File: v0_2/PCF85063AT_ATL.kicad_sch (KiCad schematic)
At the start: 4 parts, among them Q3 DMG2301L-7, U2 PCF85063ATL

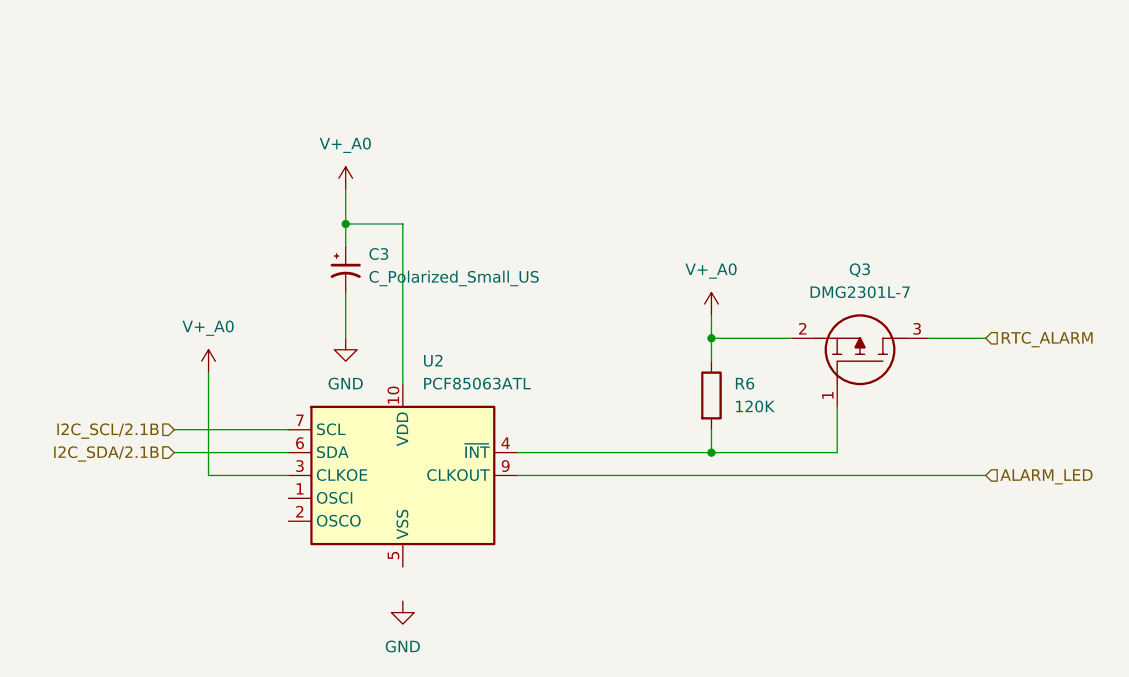
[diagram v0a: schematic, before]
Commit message: add sensor schematic
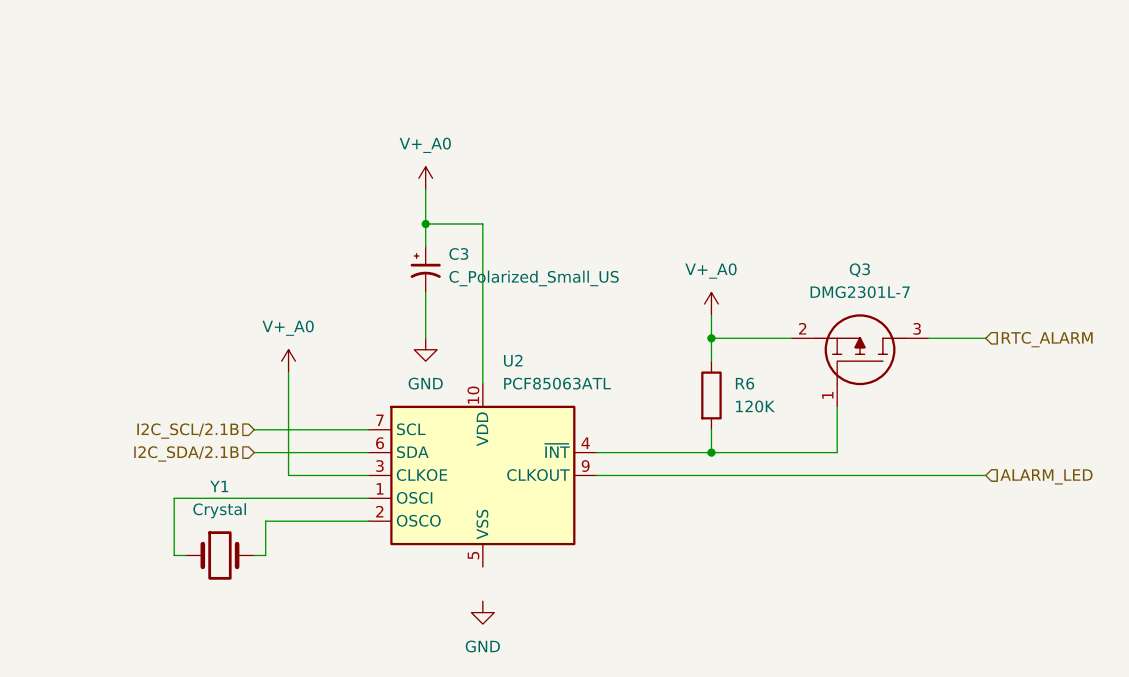
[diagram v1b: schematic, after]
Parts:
- added Y1: Crystal, symbol Device:Crystal
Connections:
- net at U2.1 (OSCI): now also Y1.1
- net at U2.2 (OSCO): now also Y1.2
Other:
- moved on the sheet: C3, U2

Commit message: schematic for enviro done
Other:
- note added: "RTC"
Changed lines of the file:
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@@
   (junction (at 121.92 74.93) (diameter 0) (color 0 0 0 0)
+  )
+  (junction (at 106.68 93.98) (diameter 0) (color 0 0 0 0)
   )
   (junction (at 153.67 100.33) (diameter 0) (color 0 0 0 0)
@@
   )
   (wire (pts (xy 121.92 74.93) (xy 121.92 71.12))
+    (stroke (width 0) (type default))
+  )
+  (wire (pts (xy 106.68 93.98) (xy 106.68 91.44))
     (stroke (width 0) (type default))
   )
@@
     (stroke (width 0) (type default))
   )
+  (wire (pts (xy 106.68 93.98) (xy 107.95 93.98))
+    (stroke (width 0) (type default))
+  )
   (wire (pts (xy 128.27 74.93) (xy 121.92 74.93))
     (stroke (width 0) (type default))
   )
-  (wire (pts (xy 106.68 102.87) (xy 106.68 91.44))
+  (wire (pts (xy 106.68 102.87) (xy 106.68 93.98))
     (stroke (width 0) (type default))
   )
@@
     (stroke (width 0) (type default))
   )
+  (text "RTC" (at 92.71 57.15 0)
+    (effects (font (face "Ubuntu") (size 3 3) (thickness 1) bold) (justify left bottom))
+  )
   (hierarchical_label "ALARM_LED" (shape input) (at 184.15 102.87 0) (fields_autoplaced)
     (effects (font (size 1.27 1.27)) (justify left))
   )
+  (hierarchical_label "V+_A0" (shape input) (at 107.95 93.98 0) (fields_autoplaced)
+    (effects (font (size 1.27 1.27)) (justify left))
+  )

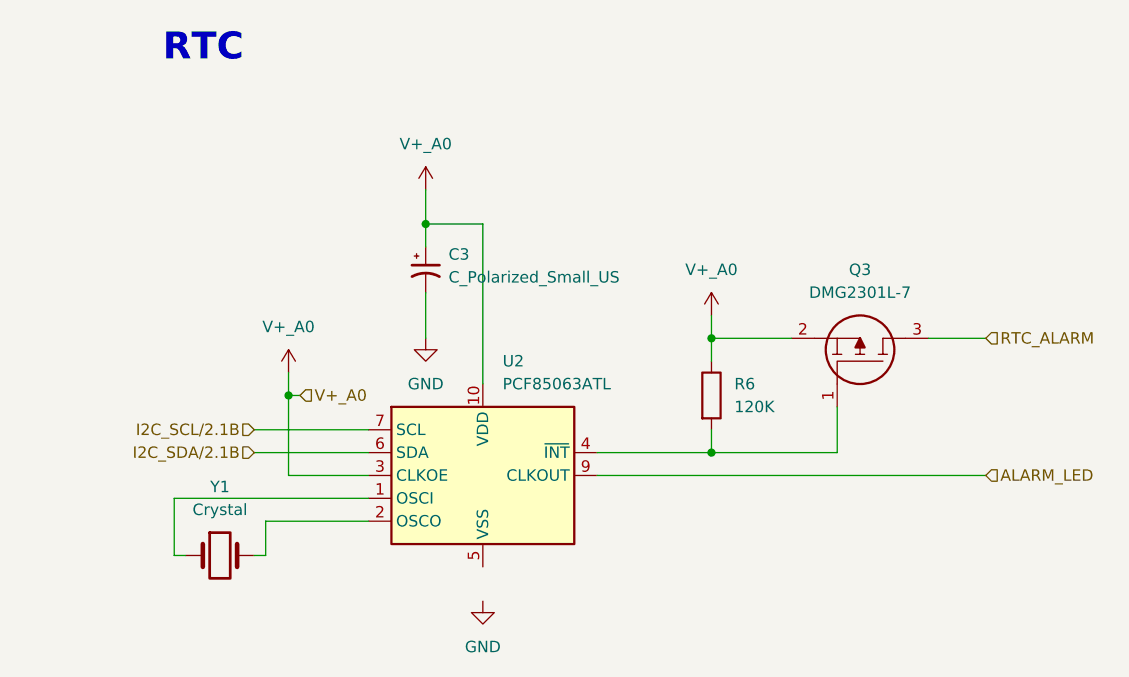
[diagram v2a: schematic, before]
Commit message: all part are added
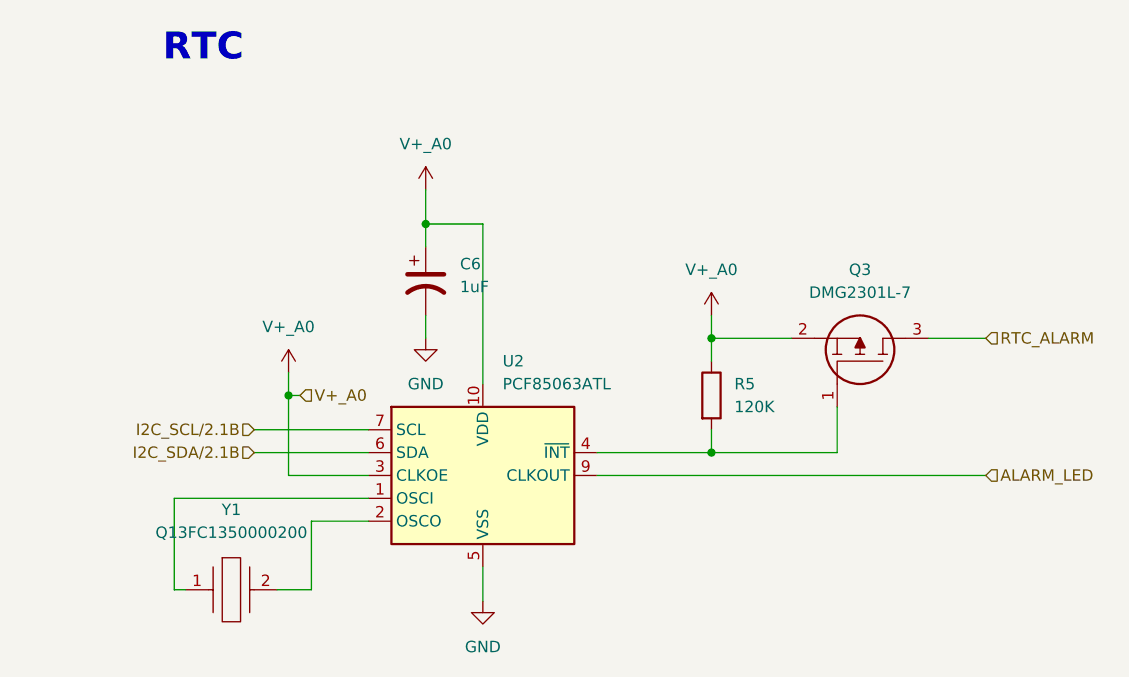
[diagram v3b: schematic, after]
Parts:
- removed C3: C_Polarized_Small_US, symbol Device:C_Polarized_Small_US
- removed R6: 120K, symbol Device:R
- removed Y1: Crystal, symbol Device:Crystal
- added C6: 1uF, Capacitor_SMD:C_0603_1608Metric, symbol Device:C_Polarized_US
- added R5: 120K, Resistor_SMD:R_0603_1608Metric, symbol Device:R
- added Y1: Q13FC1350000200, Q13FC1350000200:Q13FC1350000200, symbol Q13FC1350000200:Q13FC1350000200
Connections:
- net GND: now also U2.5 (VSS), C6.2
- net V+_A0: now also C6.1, R5.1
- net at U2.1 (OSCI): now also Y1.1
- net at U2.2 (OSCO): now also Y1.2
- net at Q3.1, U2.4 (~{INT}): now also R5.2
